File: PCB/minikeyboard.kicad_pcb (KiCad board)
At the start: 2 copper layers, 83.3 x 51.5 mm, 7 parts, among them SW1 SW_Push, SW2 SW_Push, SW3 SW_Push, SW4 SW_Push, U1 XIAO-RP2040-DIP

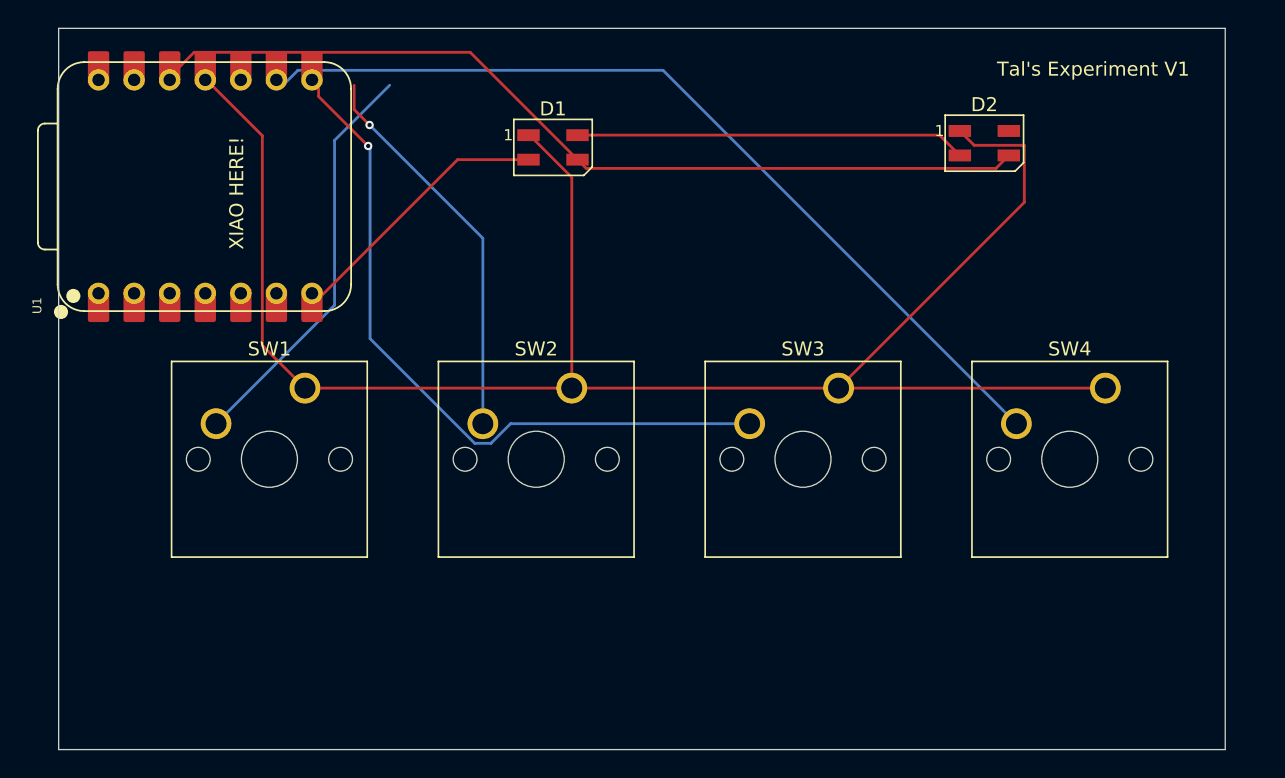
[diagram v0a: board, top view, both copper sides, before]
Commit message: Change the code from QMK to KMK and added an encoder
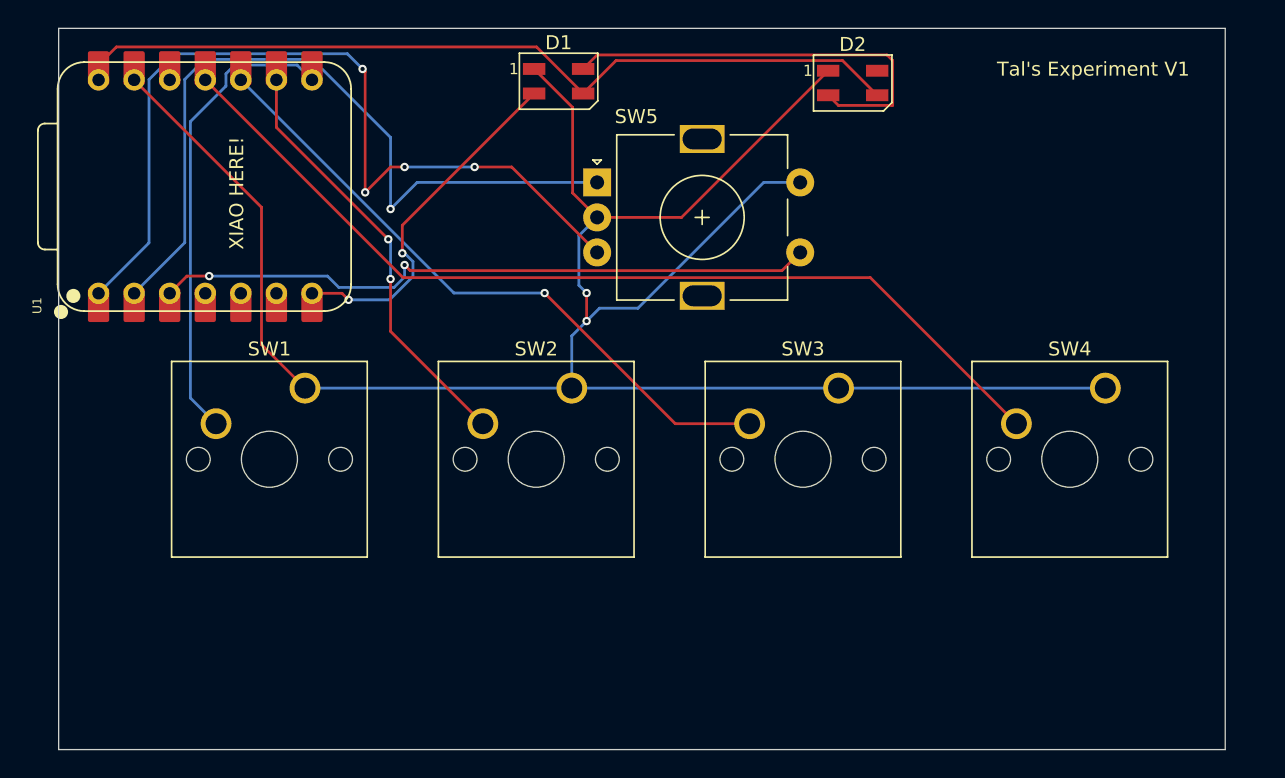
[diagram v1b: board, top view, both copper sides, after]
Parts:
- added SW5: RotaryEncoder_Switch, Rotary_Encoder:RotaryEncoder_Alps_EC11E-Switch_Vertical_H20mm, F.Cu at (156.8, 73.1)
- moved D2 10.3 mm to (175.0, 66.0)
- moved D1 4.74 mm to (154.0, 65.9)
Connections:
- U1 pad 1: unconnected-(U1-GPIO26/ADC0/A0-Pad1) -> Net-(U1-GPIO26/ADC0/A0)
- U1 pad 2: unconnected-(U1-GPIO27/ADC1/A1-Pad2) -> Net-(U1-GPIO27/ADC1/A1)
- U1 pad 3: unconnected-(U1-GPIO28/ADC2/A2-Pad3) -> Net-(U1-GPIO28/ADC2/A2)
- U1 pad 5: Net-(D1-VSS) -> unconnected-(U1-GPIO6/SDA-Pad5)
- U1 pad 7: unconnected-(U1-GPIO0/TX-Pad7) -> Net-(D1-VSS)
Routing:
- net Net-(U1-GPIO26/ADC0/A0): track 0.00 -> 61.9 mm, vias 0 -> 4
- net Net-(U1-GPIO27/ADC1/A1): track 0.00 -> 55.0 mm, vias 0 -> 1
- net Net-(U1-GPIO28/ADC2/A2): track 0.00 -> 47.7 mm, vias 0 -> 2
- net GND: track 128.8 -> 150.3 mm, vias 0 -> 2
- net Net-(D1-VSS): track 19.1 -> 25.5 mm, vias 0 -> 2
- net Net-(U1-GPIO3/MOSI): track 63.3 -> 68.1 mm
- net Net-(U1-GPIO1/RX): track 29.3 -> 33.6 mm
- net +5V: track 64.9 -> 60.6 mm
- net Net-(U1-GPIO4/MISO): track 50.4 -> 46.5 mm
- net Net-(D1-VDD): track 27.9 -> 30.8 mm
- net Net-(U1-GPIO2/SCK): track 28.0 -> 30.7 mm, vias 1 -> 2
- net unconnected-(U1-3V3-Pad12): track 0.00 -> 1.08 mm

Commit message: Add files via upload
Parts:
- D1, D2: footprint LED_SMD:LED_SK6812MINI_PLCC4_3.5x3.5mm_P1.75mm -> ledfoot:MX_SK6812MINI-E_REV
- moved D1 39.5 mm to (193.4, 62.9)
- moved D2 19.7 mm to (193.4, 73.2)
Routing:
- net Net-(D1-VSS): track 25.5 -> 91.5 mm, vias 2 -> 4
- net +5V: track 60.6 -> 83.8 mm
- net Net-(D1-VDD): track 30.8 -> 10.9 mm
- net GND: track 150.3 -> 138.7 mm
